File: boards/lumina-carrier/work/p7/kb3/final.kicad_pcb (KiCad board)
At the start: 4 copper layers, 100 x 80 mm, 116 parts, among them J1 LPJG0926HENL PoE+ RJ45 magjack, J2 1x6 2.54mm header (recovery), J3 DS1021-2x7SF11-B 2x7 male hea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, J4 DS1021-2x12SF11-B 2x12 male h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, SW1 SMD tactile switch, U1 TPS2378DDAR, U10 W5500, U20 SCT2A25STER, U21 TPS563201DDCR, U22 TPS16630PWPR, U30 ESP32-S3-WROOM-1-N8, Y10 25MHz 18pF CL crystal

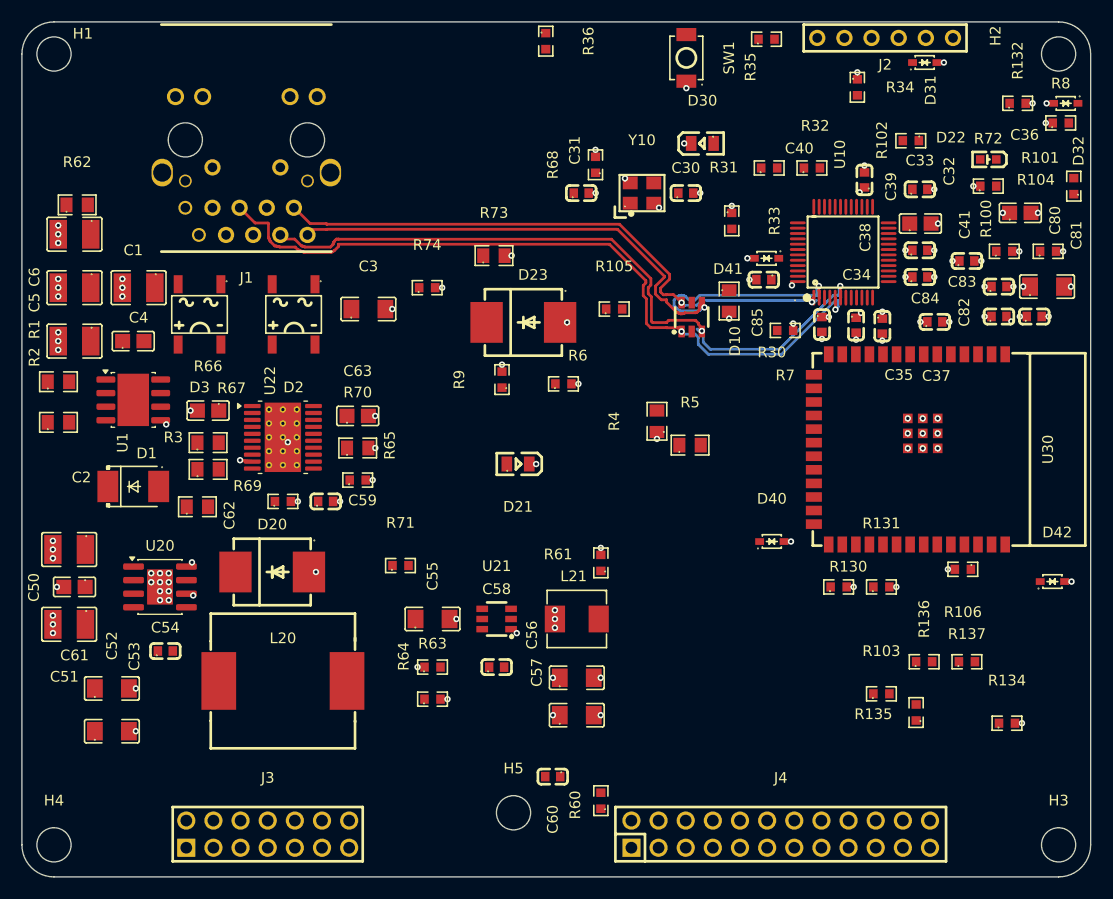
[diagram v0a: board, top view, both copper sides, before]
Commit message: ai-ee lumina-carrier: P7 partial - planes, rule areas, MDI pairs, thermal stitching (177 unrouted)
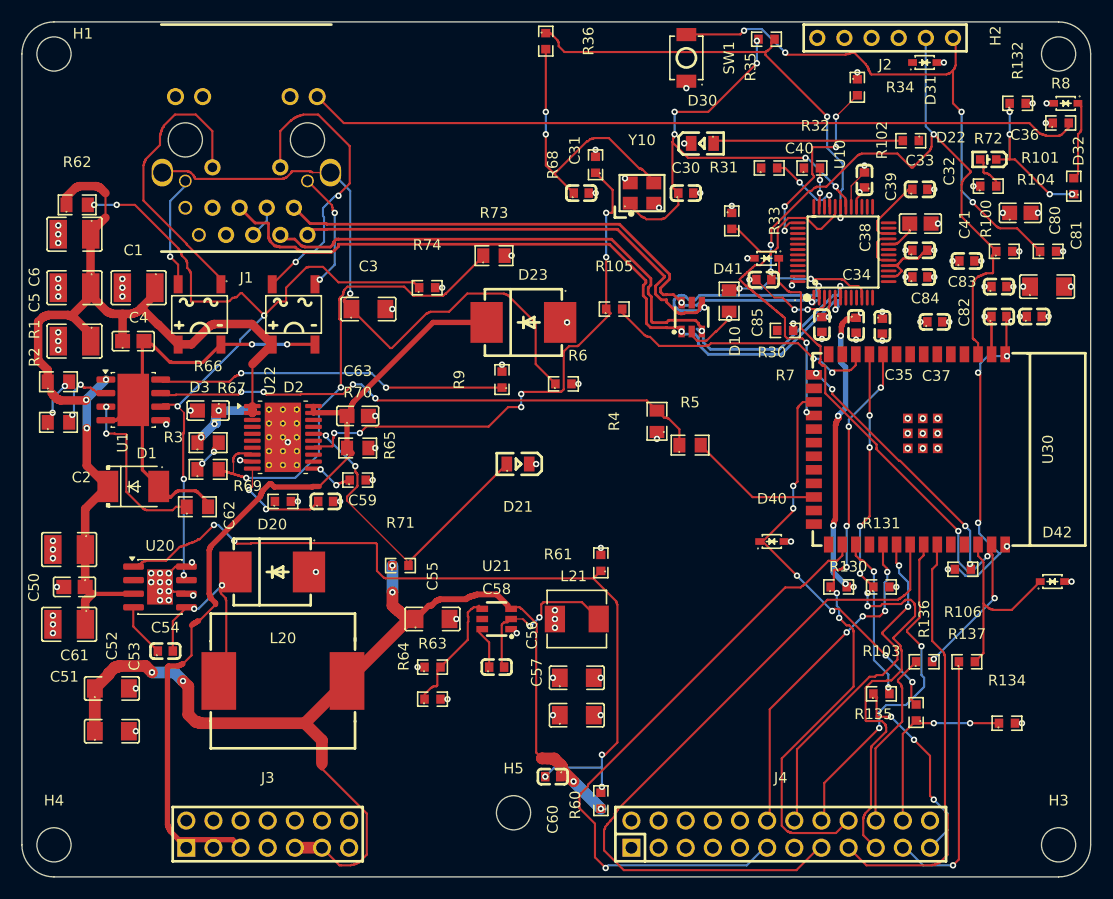
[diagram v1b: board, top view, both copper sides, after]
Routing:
- net V48_RAW: track 0.00 -> 109.7 mm, vias 0 -> 6
- net +12V: track 0.00 -> 108.0 mm, vias 0 -> 6
- net +48V_SW: track 0.00 -> 80.5 mm
- net /pwr/FB48: track 0.00 -> 76.6 mm, vias 0 -> 5
- net /poe/LED_G_A: track 0.00 -> 72.6 mm
- net /CDB: track 0.00 -> 71.8 mm, vias 0 -> 6
- net /DSPI_MOSI: track 0.00 -> 66.2 mm
- net GND: track 9.60 -> 74.1 mm, vias 96 -> 102
- net /mcu/EN: track 0.00 -> 60.1 mm, vias 0 -> 3
- net /I2C_SDA: track 0.00 -> 58.9 mm, vias 0 -> 6
- net /poe/SHIELD: track 0.00 -> 58.9 mm, vias 0 -> 1
- net /PWM6: track 0.00 -> 58.5 mm, vias 0 -> 1
- net /I2C_SCL: track 0.00 -> 57.5 mm, vias 0 -> 6
- net /ADC0: track 0.00 -> 55.0 mm, vias 0 -> 4
- net /poe/T2P_OD: track 0.00 -> 52.5 mm, vias 0 -> 4
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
